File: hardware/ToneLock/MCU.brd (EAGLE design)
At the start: 11 parts, among them U1 LD1117S33TR, U2 MP45DT02, U3 LIS3DSHTR

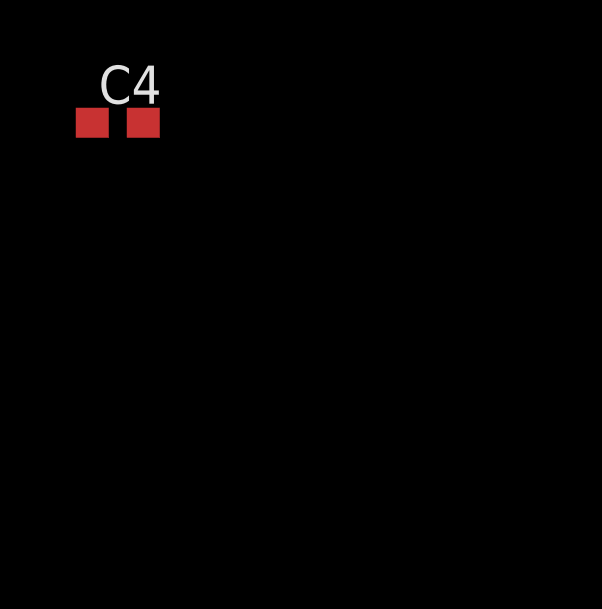
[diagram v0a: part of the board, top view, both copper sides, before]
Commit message: Renamed datasheets and Added UART pins
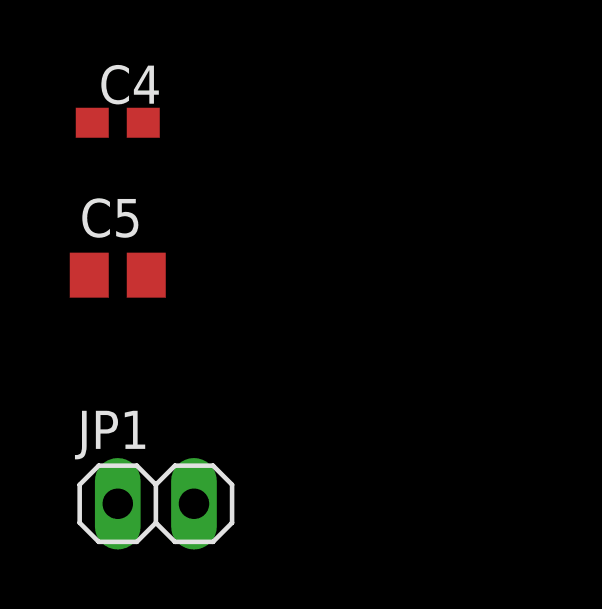
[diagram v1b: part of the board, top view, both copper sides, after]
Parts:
- added C5: 10uF, resistor:C0805
- added JP1: (no value), pinhead:1X02
- C4: value (none) -> 100nF
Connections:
- new net UART4_RX: JP1.1, U$1.24
- new net UART4_TX: JP1.2, U$1.23
- net GND: now also C5.2
- net VDD: now also C5.1
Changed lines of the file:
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@@
 </element>
 <element name="C2" library="resistor" library_urn="urn:adsk.eagle:library:348" package="C0805" package3d_urn="urn:adsk.eagle:package:23617/2" value="10uF" x="-36.83" y="-67.31"/>
-<element name="C4" library="resistor" library_urn="urn:adsk.eagle:library:348" package="C0603" package3d_urn="urn:adsk.eagle:package:23616/2" value="" x="-36.83" y="-73.66"/>
+<element name="C4" library="resistor" library_urn="urn:adsk.eagle:library:348" package="C0603" package3d_urn="urn:adsk.eagle:package:23616/2" value="100nF" x="-36.83" y="-73.66"/>
+<element name="C5" library="resistor" library_urn="urn:adsk.eagle:library:348" package="C0805" package3d_urn="urn:adsk.eagle:package:23617/2" value="10uF" x="-36.83" y="-78.74"/>
+<element name="JP1" library="pinhead" library_urn="urn:adsk.eagle:library:325" package="1X02" package3d_urn="urn:adsk.eagle:package:22435/2" value="" x="-35.56" y="-86.36"/>
 </elements>
 <signals>
@@
 <contactref element="U3" pad="12"/>
 <contactref element="C4" pad="2"/>
+<contactref element="C5" pad="2"/>
+<wire x1="-35.98" y1="-73.66" x2="-35.88" y2="-78.74" width="0" layer="19" extent="1-1"/>
 <wire x1="-37.78" y1="-67.31" x2="-35.98" y2="-73.66" width="0" layer="19" extent="1-1"/>
 <wire x1="-38.055" y1="-60.69" x2="-37.78" y2="-67.31" width="0" layer="19" extent="1-1"/>
@@
 <contactref element="U3" pad="10"/>
 <contactref element="C4" pad="1"/>
+<contactref element="C5" pad="1"/>
+<wire x1="-37.68" y1="-73.66" x2="-37.78" y2="-78.74" width="0" layer="19" extent="1-1"/>
 <wire x1="-35.88" y1="-67.31" x2="-37.68" y2="-73.66" width="0" layer="19" extent="1-1"/>
 <wire x1="-35.605" y1="-60.19" x2="-35.88" y2="-67.31" width="0" layer="19" extent="1-1"/>
@@
 <wire x1="-34.22" y1="-40.64" x2="-33.87" y2="-57.15" width="0" layer="19" extent="1-1"/>
 </signal>
+<signal name="UART4_TX">
+<contactref element="U$1" pad="23"/>
+<contactref element="JP1" pad="2"/>
+<wire x1="-11.41" y1="-26.59" x2="-34.29" y2="-86.36" width="0" layer="19" extent="1-1"/>
+</signal>
+<signal name="UART4_RX">
+<contactref element="U$1" pad="24"/>
+<contactref element="JP1" pad="1"/>
+<wire x1="-11.41" y1="-27.09" x2="-36.83" y2="-86.36" width="0" layer="19" extent="1-1"/>
+</signal>
 </signals>

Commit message: Changed UART to use USART2
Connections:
- net UART4_RX renamed USART2_RX
- net UART4_TX renamed USART2_TX
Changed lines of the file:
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@@
 <wire x1="-34.22" y1="-40.64" x2="-33.87" y2="-57.15" width="0" layer="19" extent="1-1"/>
 </signal>
-<signal name="UART4_TX">
-<contactref element="U$1" pad="23"/>
-<contactref element="JP1" pad="2"/>
-<wire x1="-11.41" y1="-26.59" x2="-34.29" y2="-86.36" width="0" layer="19" extent="1-1"/>
-</signal>
-<signal name="UART4_RX">
+<signal name="USART2_RX">
 <contactref element="U$1" pad="24"/>
 <contactref element="JP1" pad="1"/>
 <wire x1="-11.41" y1="-27.09" x2="-36.83" y2="-86.36" width="0" layer="19" extent="1-1"/>
 </signal>
+<signal name="USART2_TX">
+<contactref element="JP1" pad="2"/>
+<contactref element="U$1" pad="23"/>
+<wire x1="-11.41" y1="-26.59" x2="-34.29" y2="-86.36" width="0" layer="19" extent="1-1"/>
+</signal>
 </signals>
